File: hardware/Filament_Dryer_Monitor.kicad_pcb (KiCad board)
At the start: 4 copper layers, 81.5 x 48 mm, 87 parts, among them J2 USB_C_Receptacle_USB2.0_16P, Q1 DMP6180SK3-13, SW1 SW_RST, SW2 SW_BOOT, U1 ESP32-WROOM-32E, U2 AP66200, U3 CP2102N-Axx-xQFN28, U4 USBLC6-2SC6

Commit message: PCB layout progress before board resize
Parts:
- added REF**: MountingHole_2.5mm, MountingHole:MountingHole_2.5mm, F.Cu at (120.0, 137.8)
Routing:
- net GND: track 33.1 -> 138.4 mm, vias 22 -> 46
- net Net-(J_display1-Pin_4): track 14.6 -> 96.4 mm, vias 0 -> 1
- net Net-(J_display1-Pin_3): track 15.8 -> 80.7 mm, vias 0 -> 1
- net 3V3_MCU: track 230.3 -> 268.4 mm, vias 6 -> 11
- net 24V_PROT: track 111.4 -> 148.1 mm, vias 0 -> 3
- net /MCU/ESP_TXD0: track 9.31 -> 41.5 mm, vias 0 -> 2
- net Net-(Q_rst1-C): track 37.5 -> 69.2 mm, vias 0 -> 2
- net /MCU/ESP_RXD0: track 8.31 -> 39.4 mm, vias 0 -> 2
- net /MCU/USB_VBUS: track 14.8 -> 26.7 mm
- net Net-(J2-D--PadA7): track 2.80 -> 7.34 mm, vias 0 -> 2
- net /Power/VCC_AP66200: track 9.38 -> 10.5 mm

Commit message: Board resize in progress
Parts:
- added REF**: MountingHole_2.5mm, MountingHole:MountingHole_2.5mm, B.Cu at (114.0, 109.0)
- added REF**: MountingHole_2.5mm, MountingHole:MountingHole_2.5mm, B.Cu at (124.0, 109.0)
- added REF**: MountingHole_2.5mm, MountingHole:MountingHole_2.5mm, B.Cu at (174.0, 109.0)
- BZ1: renamed from BUZZER1; moved to F.Cu
- D6: renamed from D_buz1; moved to F.Cu
- Q6: renamed from Q_buz1; moved to F.Cu
- R27: renamed from R_buz1; moved to F.Cu
- REF**: moved to B.Cu
- moved REF** 70.2 mm to (184.0, 109.0), turned to 180 degrees
- moved TP1 65.1 mm to (131.8, 164.3)
- moved TP3 65.1 mm to (124.7, 164.3)
- moved TP2 65.1 mm to (128.3, 164.3)
- moved C1 59.2 mm to (226.1, 73.0)
- moved C11 59.2 mm to (214.2, 82.7)
- moved C3 59.2 mm to (230.4, 78.3)
- moved C6 59.2 mm to (219.0, 79.0)
- moved C7 59.2 mm to (236.5, 75.5)
- moved C8 59.2 mm to (219.0, 82.7)
- moved D1 59.2 mm to (222.6, 88.9)
- moved J1 59.2 mm to (233.7, 94.3)
- moved L1 59.2 mm to (224.8, 81.1)
- moved Q1 59.2 mm to (221.0, 97.6)
- moved R1 59.2 mm to (226.1, 76.5)
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- renumbered Cen1 to C1, Cout3 to C10, Cmcu1 to C11, C_vdd1 to C12, C_vdd2 to C13, C_reg1 to C14, C_en1 to C15, C_esp1 to C16, C_esp2 to C17, C_esp3 to C18, C_ntc1 to C19, Cvcc1 to C2, Cbst1 to C3, Cff1 to C4, Cin1 to C5, Cout1 to C6, Cin2 to C7, Cout2 to C8, Cin3 to C9, Dz1 to D1, TVS1 to D2, D_led1 to D3, D_heat1 to D4, D_fan1 to D5, J_dc1 to J1, J_sens1 to J3, J_display1 to J4, J_heat1 to J5, J_fan2 to J6, J_ntc1 to J7, Q_boot1 to Q2, Q_rst1 to Q3, Q_heat1 to Q4, Q_fan1 to Q5, Ren_top1 to R1, R_cc2 to R10, R_cc1 to R11, R_en1 to R12, R_io0 to R13, R_pu_sda1 to R14, R_pu_scl1 to R15, R_s_scl1 to R16, R_s_sda1 to R17, R_led1 to R18, R_btn1 to R19, Ren_bot1 to R2, R_g_heat1 to R20, R_pd_heat1 to R21, R_btn2 to R22, R_btn3 to R23, R_btn4 to R24, R_g_fan1 to R25, R_pd_fan1 to R26, R_ntc1 to R28, Rg1 to R3, Rpg1 to R4, Rfb_top1 to R5, Rfb_bot1 to R6, R_vbus_top1 to R7, R_vbus_bot1 to R8, R_rst1 to R9, SW_onoff1 to SW3, SW_m1 to SW4, SW_up1 to SW5, SW_down1 to SW6, TP7 to TP5, TP5 to TP6, TP6 to TP7, U2 to U1, U3 to U2, U4 to U3, U1 to U4
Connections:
- U3 pad 1: Net-(J2-D+-PadA6) -> Net-(J2-D--PadA7)
- U3 pad 3: Net-(J2-D--PadA7) -> Net-(J2-D+-PadA6)
- U3 pad 4: /MCU/USB_DM -> /MCU/USB_DP
- U3 pad 6: /MCU/USB_DP -> /MCU/USB_DM
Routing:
- net 3V3_MCU: track 268.4 -> 53.8 mm, vias 11 -> 5
- net 24V_PROT: track 148.1 -> 0.00 mm, vias 3 -> 0
- net GND: track 138.4 -> 25.5 mm, vias 46 -> 13
- net HEATER_PWM: track 73.0 -> 0.00 mm
- net FAN_PWM: track 62.6 -> 0.00 mm
- net /MCU/ESP_TXD0: track 41.5 -> 0.00 mm, vias 2 -> 0
- net /MCU/ESP_RXD0: track 39.4 -> 0.00 mm, vias 2 -> 0
- net /Power/3V3_BUCK: track 26.5 -> 0.00 mm
- net Net-(J3-Pin_3): track 80.7 -> 102.2 mm, vias 1 -> 2
- net Net-(Q3-C): track 69.2 -> 52.3 mm
- net BTN_DOWN: track 56.3 -> 72.6 mm
- net BTN_UP: track 70.6 -> 86.9 mm
- net Net-(D4-A): track 12.1 -> 0.00 mm
- net Net-(J3-Pin_2): track 96.4 -> 107.9 mm, vias 1 -> 2
- net /MCU/USB_DM: track 11.3 -> 22.7 mm
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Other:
- board size 81.5 x 48 mm -> 98 x 58 mm

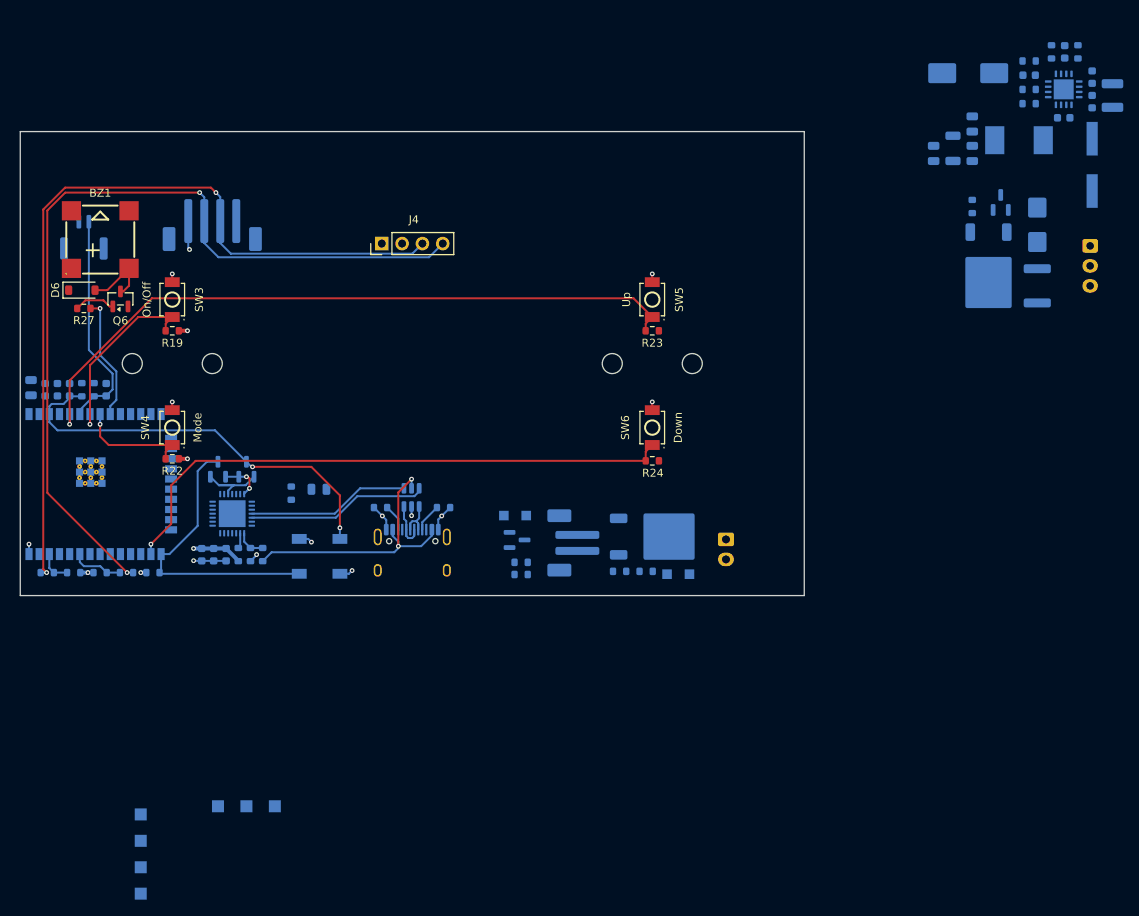
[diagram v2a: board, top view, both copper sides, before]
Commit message: Update README: GPIO map (fan/up/down pins), button description, board size under revision
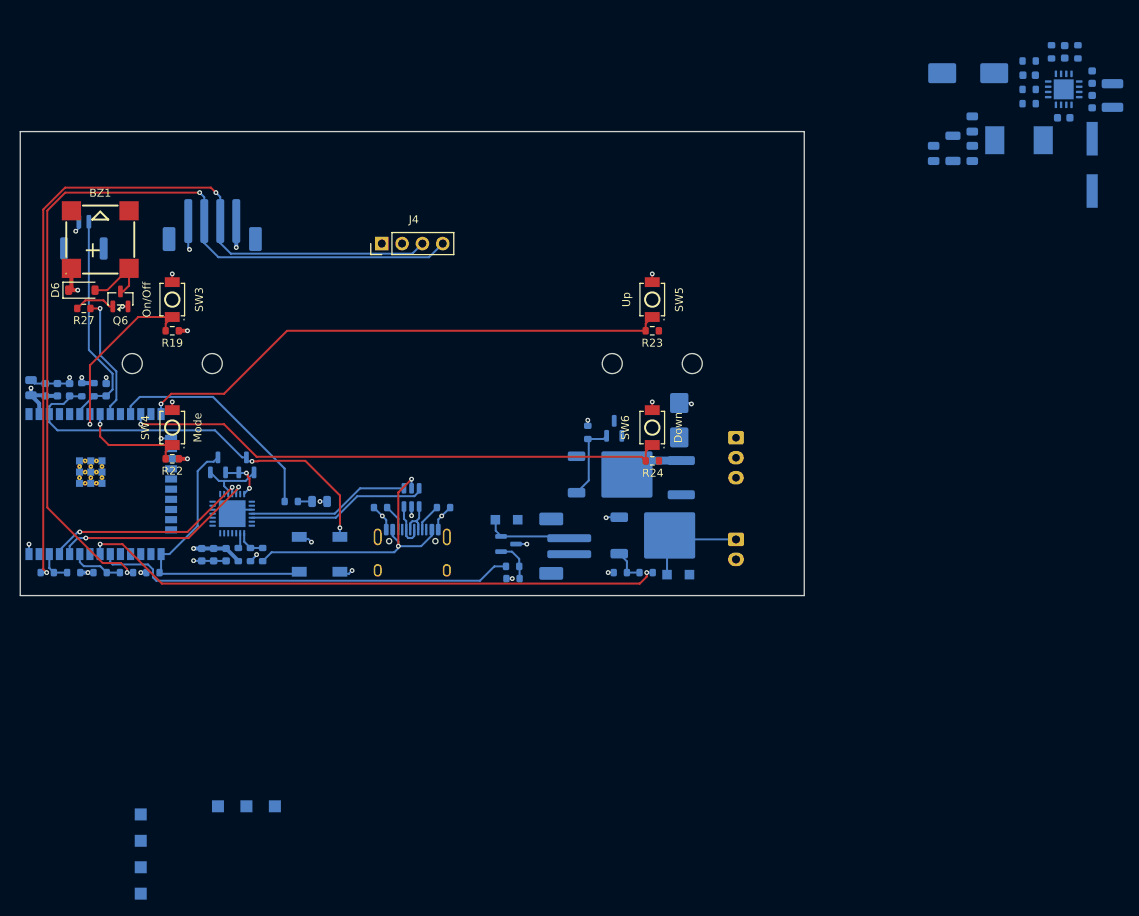
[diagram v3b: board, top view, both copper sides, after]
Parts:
- moved D1 56.0 mm to (174.2, 117.1)
- moved R3 55.7 mm to (170.9, 117.6)
- moved Q1 52.9 mm to (174.6, 122.9), turned to 0 degrees
- moved D2 51.0 mm to (182.4, 116.1)
- moved F1 50.6 mm to (182.6, 123.3)
- moved J1 50.3 mm to (189.5, 118.3)
- moved D3 1.53 mm to (137.4, 126.2)
- moved J5 1.25 mm to (189.5, 131.0)
- moved D5 1.19 mm to (160.8, 128.5)
- moved Q5 1.18 mm to (161.0, 131.6)
- moved R25 1.18 mm to (161.5, 134.4)
- moved R26 1.14 mm to (161.6, 135.9)
- moved J6 1.10 mm to (168.1, 131.8)
- moved R18 1.04 mm to (133.9, 126.2), turned to 180 degrees
- moved Q2 0.54 mm to (124.7, 121.7)
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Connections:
- U4 pad 10: FAN_PWM -> unconnected-(U4-IO25-Pad10)
- U4 pad 12: unconnected-(U4-IO27-Pad12) -> BTN_DOWN
- U4 pad 14: unconnected-(U4-IO12-Pad14) -> BTN_UP
- U4 pad 26: BTN_DOWN -> unconnected-(U4-IO4-Pad26)
- U4 pad 30: unconnected-(U4-IO18-Pad30) -> FAN_PWM
- U4 pad 5: BTN_UP -> unconnected-(U4-SENSOR_VN-Pad5)
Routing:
- net HEATER_PWM: track 0.00 -> 73.2 mm, vias 0 -> 2
- net 3V3_MCU: track 53.8 -> 121.8 mm, vias 5 -> 9
- net FAN_PWM: track 0.00 -> 52.8 mm
- net /MCU/LED_DRV: track 0.00 -> 28.6 mm
- net /MCU/ESP_RXD0: track 0.00 -> 26.3 mm, vias 0 -> 2
- net /MCU/ESP_TXD0: track 0.00 -> 26.2 mm, vias 0 -> 2
- net GND: track 25.5 -> 45.6 mm, vias 13 -> 25
- net BTN_UP: track 86.9 -> 67.7 mm
- net Net-(D4-A): track 0.00 -> 13.3 mm
- net Net-(D5-A): track 0.00 -> 11.0 mm
- net /Power/GATE_Q1: track 0.00 -> 9.91 mm
- net /Power/FUSE_OUT: track 0.00 -> 7.51 mm
- net Net-(Q5-G): track 0.00 -> 5.13 mm
- net Net-(Q4-G): track 0.00 -> 4.34 mm
- net BTN_DOWN: track 72.6 -> 68.6 mm
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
